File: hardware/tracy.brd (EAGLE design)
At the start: 82.8 x 56 mm, 62 parts, among them IC1 SIM900, J1 U.FL, Q1 si2305cd, Q2 8MHz 18pF, Q3 IRFR5305, T1 BC846, U1 SPX5205 3v3, X3 MKDSN1,5/4-5,08, Y1 32768Hz CFPX-217 12.5pF

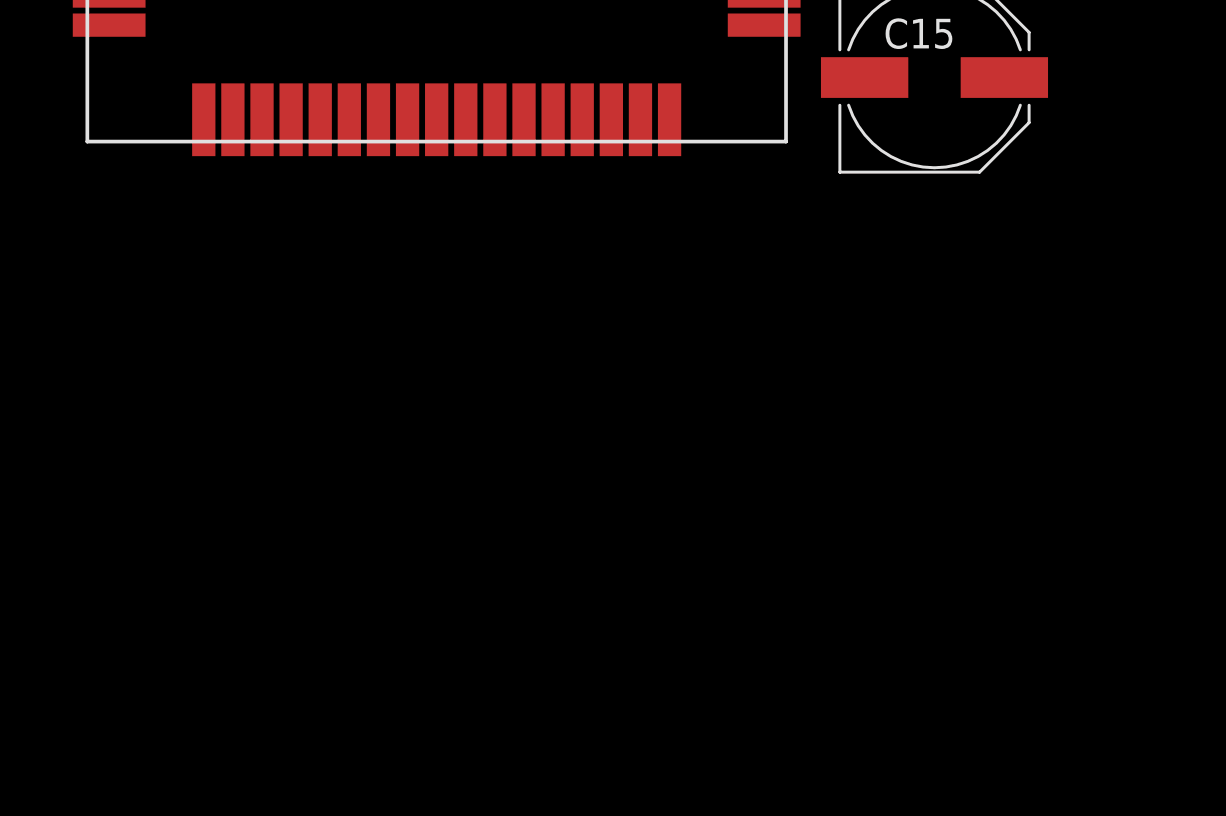
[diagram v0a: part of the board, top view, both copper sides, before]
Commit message: create sim card reader footprint
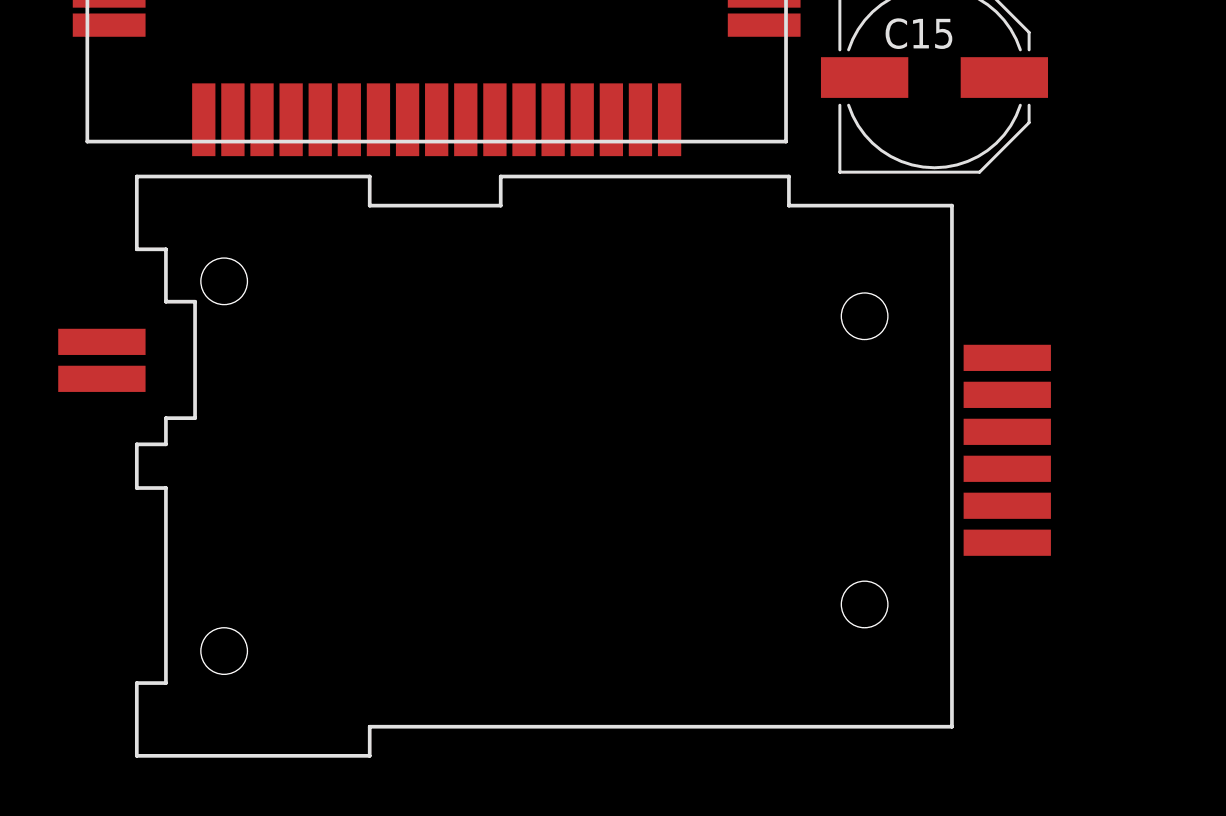
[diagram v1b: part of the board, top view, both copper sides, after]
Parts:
- added U$3: SIMLOCKC707_10M006_000_2, Simplex-Connectors:SIMLOCK_C707_10M006
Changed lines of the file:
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@@
 <element name="C15" library="SparkFun-Capacitors" package="PANASONIC_D" value="10uF" x="-39.6" y="-9.5"/>
 <element name="IC1" library="sim900" package="SIM900" value="SIM900" x="-56.7" y="0.3"/>
+<element name="U$3" library="Simplex-Connectors" package="SIMLOCK_C707_10M006" value="SIMLOCKC707_10M006_000_2" x="-64" y="-29.2"/>
 </elements>
 <signals>

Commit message: sch work
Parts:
- removed C15: 10uF, SparkFun-Capacitors:PANASONIC_D
- removed C2, C20: 10uF, rcl:C1206
- removed C21, C22: 33pF, rcl:C0805
- removed D2: SB560, diode:C1702-05
- removed JP1: i2c, SparkFun-Connectors:1X04
- removed JP2: thermistor, SparkFun-Connectors:1X02
- removed JP5: debug, SparkFun-Connectors:1X07
- removed JP9: digital2, SparkFun-Connectors:1X07
- removed LED1: green, led:CHIP-LED0805
- removed LED2: orange, led:CHIP-LED0805
- removed Q1: si2305cd, Simplex-DiscreteSemi:SOT23-3_POWER
- removed Q2: 8MHz 18pF, Omat_komponentit:CRYSTAL_5X3.2
- removed Q3: IRFR5305, transistor-power:D-PAK_TO252AA
- removed R10, R27: 1K, rcl:R0805W
- removed R12, R13: 320, rcl:R0805W
- removed R16, R3: 100k, rcl:R0805W
- removed R19, R8: 10k, rcl:R0805W
- removed R25: 2M, rcl:R0805W
- removed R26: 240k, rcl:R0805W
- removed R4, R5, R6, R7: 4.7k, rcl:R0805W
- removed T1: BC846, transistor:SOT23
- removed U$4: INDUCTOR, Simplex-rlc:L0805W
- removed X3: MKDSN1,5/4-5,08, con-phoenix-508:MKDSN1,5/4-5,08
- added C12: 4u7, rcl:C0805
- added C13: 100n, rcl:C0805
- added C14: 22p, rcl:C0805
- added C16: 47uF, rcl:C1206
- added C25, C26, C29: 100nF, rcl:C0805
- added C27, C28: 4u7, rcl:C1206
- added C30: 10uF, rcl:C1206
- added C32: 1uF, rcl:C0805
- added D1: DIODE-SCHOTTKY_, SparkFun-DiscreteSemi:SMA-DIODE
- added J2: U.FL, SparkFun-Connectors:U.FL
- added LED3: orange, led:CHIP-LED0805
- added Q4: si2305cd, Simplex-DiscreteSemi:SOT23-3_POWER
- added R11: 3k, rcl:R0805W
- added R14: NA/10k, rcl:R0805W
- added R15: 1k1, rcl:R0805W
- added R17, R23, R9: 10k, rcl:R0805W
- added R18: 47k, rcl:R0805W
- added R20: 4k7, rcl:R0805W
- added R21: 100k, rcl:R0805W
- added T2: BC846, transistor:SOT23
- added U$10: bead, Simplex-rlc:L0805W
- added U$6: BQ24072, Simplex-ICs:S-PVQFN-N16
- added U$8: 22, Simplex-rlc:YC164
- added U$9: RESETTABLE, Simplex-Fuses:1210
- added U3: TC1014 2V8, SparkFun:SOT23-5
- C19: value 100nF -> 10uF; device rcl:C0805 -> rcl:C1206
- R2: value 10k -> 470
- U$2: value RESETTABLE -> 470; device Simplex-Fuses:1210 -> Simplex-rlc:YC164
- U$5: value INDUCTOR -> bead
- moved C19 220.1 mm to (-128.1, -54.0), turned to 0 degrees
- moved U$2 195.3 mm to (-146.3, -81.2), turned to 0 degrees
- moved R2 184.8 mm to (-150.5, -81.1), turned to 0 degrees
- moved U$7 48.3 mm to (64.5, 52.2)
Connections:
- net CS renamed P4.6
- net MOSI renamed P4.1
- net VBUS renamed 41
- net VUSB renamed 42
- removed net EN: R8.1, U$1.20
- removed net LED: R10.2, U$1.36
- removed net MISO: U$1.31
- removed net N$11: R6.2, U$1.34
- removed net N$12: R13.1, U2.P$9
- removed net N$13: R7.2, U$1.33
- removed net N$14: Q1.1, R3.1, R8.2
- removed net N$15: U$5.1
- removed net N$16: R12.1, U2.P$10
- removed net N$17: C22.2, Q2.P$1, U$1.46
- removed net N$18: R13.2
- removed net N$19: R12.2
- removed net N$23: C21.2, Q2.P$2, U$1.45
- removed net N$28: Q3.1, R2.2
- removed net N$37: Q1.3, U$4.1
- removed net N$39: LED2.C, R27.2
- removed net PU.0: U$1.38
- removed net PU.1: U$1.40
- removed net PUR: U$1.39
- removed net PV+: Q3.3, R19.1, R22.1, X3.4
- removed net RX: JP5.5, R6.1
- removed net SCK: LED2.A, U$1.32
- removed net SCL: JP1.1, R4.2, U$1.3
- removed net SDA: JP1.2, R5.2, U$1.4
- removed net SENSE: D2.A, Q3.4
- removed net TX: JP5.6, R7.1
- removed net VBAT_GND: JP2.1, X3.1, X3.2
- removed net VCC: C17.2, C8.2, C9.2, JP5.4, Q1.2, R3.2, R34.2, U$1.11, U$1.28, U$1.7
- removed net VCC_EN: C20.1, JP1.3, JP9.6, R4.1, R5.1, U$4.2
- new net 2V8: C17.2, C29.1, C30.1, C8.2, C9.2, R34.2, U$1.11, U$1.28, U$1.7, U3.5
- new net 3V3_EN: U1.3
- new net 46: U$1.46
- new net 5V: U$9.P$1
- new net 5V_IN: D1.C, R22.1, U$6.13
- new net BAT: C27.1, U$6.2
- new net CE: U$6.4
- new net CTS: IC1.7
- new net DTR: IC1.3
- new net GPRS_EN: R23.1
- new net GPRS_POW: R20.2
- new net GPRS_RX: IC1.10, U$2.7
- new net GPRS_TX: IC1.9, U$2.8
- new net GPS_RX: U$2.5, U2.P$10
- new net GPS_TX: R2.1, U$2.6, U2.P$9
- new net N$20: D1.A, U$9.P$2
- new net N$21: LED3.C, U$6.9
- new net N$22: LED3.A, R9.2
- new net N$27: R11.1, U$6.16
- new net N$29: R14.1, U$6.1
- new net N$30: C12.2, IC1.26
- new net N$32: C13.2, IC1.30, U$3.VCC
- new net N$33: R15.1, U$6.12
- new net N$34: U$3.CLK, U$8.1
- new net N$35: U$3.RST, U$8.3
- new net N$36: U$3.IO, U$8.2
- new net N$38: IC1.32, U$8.8
- new net N$40: IC1.33, U$8.6
- new net N$41: C14.2, IC1.31, U$8.7
- new net N$42: IC1.34, R17.2, U$3.LOCK_1
- new net N$43: IC1.15, R17.1
- new net N$44: IC1.1, T2.3
- new net N$45: R18.2, R20.1, T2.1
- new net N$46: IC1.60, J2.P$3
- new net N$48: Q4.1, R21.1, R23.2
- new net N$49: Q4.3, U$10.1
- new net N$50: C32.1, U3.4
- new net P4.7: U$1.36
- new net P6.2: U$1.3
- new net P6.3: U$1.4
- new net RI: IC1.4
- new net RTS: IC1.8
- net +3V3: now also U$5.1; no longer C2.1
- net GND: now also C12.1, C13.1, C14.1, C16.2, C25.2, C26.2, C27.2, C28.2, C29.2, C30.2, C32.2, J2.P$1, J2.P$2, R11.2, R14.2, R15.2, R18.1, R2.2, T2.2, U$3.GND, U$3.LOCK_2, U$6.15, U$6.6, U$6.8, U3.2; no longer C2.2, C20.2, C21.1, C22.1, JP1.4, JP5.1, JP5.7, JP9.7, LED1.C, R26.2, R27.1, T1.2
- net N$1: now also U$1.32, U$2.3; no longer LED1.A, R10.1
- net N$3: now also U$1.31, U$2.4; no longer R16.1, T1.1
- net N$4: now also U$1.33, U$2.2; no longer D2.C
- net N$5: now also U$1.34, U$2.1; no longer R19.2, R2.1, T1.3
- net P1.0: no longer JP9.1
- net P1.1: no longer JP9.2
- net P1.2: no longer JP9.3
- net P1.3: no longer JP9.4
- net P2.0: now also U$1.20; no longer R16.2
- net P4.0: no longer JP9.5
- net P5.0: no longer JP2.2
- net P6.0: no longer C19.1, R25.2, R26.1
- net RST: no longer JP5.2
- net TEST: no longer JP5.3
- net VBAT: now also C16.1, C19.1, C25.1, C26.1, U$10.2; no longer R25.1, U$2.P$1, X3.3
- net VIN: now also C28.1, Q4.2, R21.2, R9.1, U$6.10, U$6.5, U3.1, U3.3; no longer U$2.P$2, U1.3
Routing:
- net VBAT: track 186.7 -> 0.00 mm, vias 3 -> 0
- net PV+: track 167.1 -> 0.00 mm, vias 3 -> 0
- net P5.1: track 154.2 -> 0.00 mm, vias 5 -> 0
- net P5.0: track 127.9 -> 0.00 mm, vias 3 -> 0
- net VCC: track 107.7 -> 0.00 mm, vias 4 -> 0
- net VCC_EN: track 65.7 -> 0.00 mm, vias 2 -> 0
- net GND: track 63.1 -> 0.00 mm, vias 50 -> 0
- net RST: track 55.8 -> 0.00 mm, vias 4 -> 0
- net P2.0: track 53.3 -> 0.00 mm
- net P1.7: track 51.0 -> 0.00 mm
- net TEST: track 50.5 -> 0.00 mm, vias 4 -> 0
- net P1.5: track 49.7 -> 0.00 mm
- net P1.4: track 47.1 -> 0.00 mm
- net P4.1: track 41.9 -> 0.00 mm, vias 4 -> 0
- net MISO: track 40.4 -> 0.00 mm, vias 4 -> 0
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- removed copper zone on layer 1, net GND
- removed copper zone on layer 16, net GND
- removed copper zone on layer 1, net VBAT_GND
- removed copper zone on layer 16, net VBAT_GND
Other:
- board text removed: "1.0"
- board text removed: "1.1"
- board text removed: "1.2"
- board text removed: "1.3"
- board text removed: "12v bat"
- board text removed: "15-36v pv cell"
- board text removed: "4.0"
- board text removed: "bat"
- board text removed: "chg"
- board text removed: "debug"
- board text removed: "digital"
- board text removed: "en"
- board text removed: "gnd"
- board text removed: "i2c"
- board text removed: "pv"
- board text removed: "rst"
- board text removed: "rx"
- board text removed: "s0"
- board text removed: "s1"
- board text removed: "s2"
- board text removed: "sc rev 03 Petre Rodan 201308"
- board text removed: "scl"
- board text removed: "sda"
- board text removed: "test"
- board text removed: "th"
- board text removed: "tx"
- board text removed: "vcc"

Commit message: daily snapshot
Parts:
- removed C16: 47uF, rcl:C1206
- removed C25: 100nF, rcl:C0805
- added C2: 100nF, rcl:C0805
- added R3: 2M, rcl:R0805W
- added R4: 240k, rcl:R0805W
- added R5: 4k7, rcl:R0805W
- added U$17: battery, Simplex-Connectors:0530480401
- added U$18: 22, Simplex-rlc:YC164
- added U$19: power_in, Simplex-Connectors:0530480401
- added U$20: debug, Simplex-Connectors:0530470610
- C18: value 100nF -> NA 100nF
- C19: value 10uF -> 47uF
- U$8: value 22 -> SMF05C; device Simplex-rlc:YC164 -> Simplex-DiscreteSemi:SC-88
- moved U$8 91.2 mm to (-156.7, -104.7)
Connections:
- removed net N$29: R14.1, U$6.1
- removed net N$38: IC1.32, U$8.8
- removed net N$40: IC1.33, U$8.6
- removed net N$41: C14.2, IC1.31, U$8.7
- new net N$10: IC1.66
- new net N$11: IC1.52
- new net N$12: R5.1, U$19.2
- new net N$17: IC1.31, U$18.8
- new net N$18: IC1.32, U$18.7
- new net N$19: IC1.33, U$18.6
- new net PW_EN: R5.2
- new net PW_RAW: R22.1, U$19.1
- new net TS: R14.1, U$17.1, U$6.1
- net 2V8: now also U$20.4
- net 5V: now also U$19.4
- net 5V_IN: no longer R22.1
- net BAT: now also R3.1, U$17.4
- net GND: now also C2.2, R4.2, U$17.2, U$17.3, U$19.3, U$20.1, U$8.2; no longer C16.2, C25.2
- net N$32: now also U$8.3
- net N$34: now also U$18.2, U$8.4; no longer U$8.1
- net N$35: now also U$18.3, U$8.6; no longer U$8.3
- net N$36: now also C14.2, U$18.1, U$8.5; no longer U$8.2
- net N$42: now also U$8.1
- net P4.0: now also U$20.6
- net P4.1: now also U$20.5
- net P6.2: now also C2.1, R3.2, R4.1
- net RST: now also U$20.2
- net TEST: now also U$20.3
- net VBAT: no longer C16.1, C25.1

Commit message: daily snapshot
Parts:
- moved R5 289.5 mm to (94.5, 6.60)
- moved U$17 283.8 mm to (92.6, 20.5), turned to 180 degrees
- moved U$19 283.0 mm to (90.2, 8.70), turned to 180 degrees
- moved R4 261.6 mm to (75.9, 33.9), turned to 90 degrees
- moved R3 256.9 mm to (78.0, 33.9), turned to 270 degrees
- moved C2 256.7 mm to (73.8, 33.9), turned to 90 degrees
- moved D1 253.0 mm to (83.3, 12.5), turned to 90 degrees
- moved C27 242.2 mm to (87.7, 26.0), turned to 90 degrees
- moved C28 235.8 mm to (79.1, 17.5), turned to 90 degrees
- moved R2 235.3 mm to (53.1, 36.9), turned to 180 degrees
- moved U$2 235.1 mm to (57.3, 36.3), turned to 90 degrees
- moved C29 230.9 mm to (72.6, 7.20), turned to 90 degrees
- moved U$8 230.4 mm to (28.7, 32.1)
- moved U3 229.0 mm to (67.8, 7.20), turned to 180 degrees
- moved C30 226.3 mm to (70.5, 7.20), turned to 90 degrees
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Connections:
- net N$30 renamed VRTC
- net N$32 renamed SIM_VCC
- net N$34 renamed SIMLOCK_CLK
- net N$35 renamed SIMLOCK_RST
- net N$36 renamed SIMLOCK_IO
- net N$44 renamed PWRKEY
- net GND: now also U2.12, U2.19, U2.3, U2.8; no longer U2.P$12, U2.P$19, U2.P$3, U2.P$8
- net GPS_RX: now also U2.10; no longer U2.P$10
- net GPS_TX: now also U2.9; no longer U2.P$9
- net N$31: now also U2.2; no longer U2.P$2
- net N$8: now also U2.1; no longer U2.P$1
- net N$9: now also U2.11; no longer U2.P$11
- net VBACKUP: now also U2.4; no longer U2.P$4
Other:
- board size 82.8 x 56 mm -> 100 x 80 mm

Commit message: daily snapshot
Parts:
- IC1: device sim900:SIM900 -> Simplex-ICs:SIM900
- R2: value 470 -> 2k2
- U$20: value debug -> MOLEX_6VERTICAL
- moved R15 72.8 mm to (14.9, 1.80), turned to 180 degrees
- moved R9 71.0 mm to (14.9, 7.10), turned to 180 degrees
- moved LED3 68.9 mm to (14.9, 8.90), turned to 270 degrees
- moved R11 67.0 mm to (21.1, 1.90), turned to 180 degrees
- moved C28 65.6 mm to (14.9, 4.00), turned to 0 degrees
- moved U$17 65.3 mm to (29.2, 4.70), flipped to the bottom, turned to 0 degrees
- moved C29 63.7 mm to (8.90, 8.60), turned to 180 degrees
- moved C27 63.2 mm to (27.3, 7.50), turned to 0 degrees
- moved U$6 63.1 mm to (21.8, 8.70)
- moved C32 62.0 mm to (3.10, 1.90), turned to 180 degrees
- moved C30 61.6 mm to (8.90, 6.50), turned to 180 degrees
- moved R5 59.9 mm to (34.8, 11.0)
- moved U3 59.1 mm to (8.90, 2.90)
- moved U$19 58.0 mm to (32.3, 4.70), turned to 0 degrees
- moved R22 56.9 mm to (23.5, 46.2), flipped to the bottom
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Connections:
- removed net N$10: IC1.66
- removed net N$11: IC1.52
- new net P1.6: U$1.20
- net GND: now also R2.1, U$6.TH; no longer R2.2
- net GPS_TX: no longer R2.1
- net N$5: now also R2.2
- net P2.0: no longer U$1.20
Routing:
- net VIN: track 0.00 -> 33.4 mm
- net VBAT: track 0.00 -> 11.1 mm
- net N$49: track 0.00 -> 9.36 mm
- net TS: track 0.00 -> 9.22 mm
- net 5V_IN: track 0.00 -> 7.65 mm
- net N$33: track 0.00 -> 7.14 mm
- net BAT: track 0.00 -> 6.48 mm
- net GND: track 0.00 -> 5.68 mm
- net N$45: track 0.00 -> 4.24 mm
- net N$48: track 0.00 -> 4.23 mm
- net N$50: track 0.00 -> 4.02 mm
- net N$21: track 0.00 -> 4.01 mm
- net SIM_VCC: track 0.00 -> 3.80 mm
- net VRTC: track 0.00 -> 3.40 mm
- net N$20: track 0.00 -> 3.27 mm
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- added copper zone on layer 1, net GND
